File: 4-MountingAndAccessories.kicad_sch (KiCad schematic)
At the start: 16 parts, among them J401 Spring Contact

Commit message: schematics: heavy BOM optimization, many small changes, filling missing fields, improving symbols and everything
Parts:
- H401, H402, H403, H404: Source (none) -> -
- H413: Source (none) -> Mouser
- J401: Source (none) -> TME
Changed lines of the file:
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@@
 	(title_block
 		(title "Mounting, hardware and accessories")
-		(date "2024-02-08")
+		(date "2024-02-15")
 		(rev "3.0")
 		(company "Arx")
@@
 			)
 		)
-		(property "Source" ""
+		(property "Source" "TME"
+			(at 186.69 48.895 0)
+			(effects
+				(font
+					(size 1.27 1.27)
+				)
+				(hide yes)
+			)
+		)
+		(property "Field-1" ""
 			(at 186.69 48.895 0)
 			(effects
@@
 			)
 		)
+		(property "Field-1" ""
+			(at 165.1 115.57 0)
+			(effects
+				(font
+					(size 1.27 1.27)
+				)
+				(hide yes)
+			)
+		)
 		(instances
 			(project "2023_PiezoPreamp"
@@
 			)
 		)
-		(property "Source" ""
+		(property "Source" "-"
+			(at 82.55 64.135 0)
+			(effects
+				(font
+					(size 1.27 1.27)
+				)
+				(hide yes)
+			)
+		)
+		(property "Field-1" ""
 			(at 82.55 64.135 0)
 			(effects
@@
 			)
 		)
-		(property "Source" ""
+		(property "Source" "-"
+			(at 83.82 46.99 0)
+			(effects
+				(font
+					(size 1.27 1.27)
+				)
+				(hide yes)
+			)
+		)
+		(property "Field-1" ""
 			(at 83.82 46.99 0)
 			(effects
@@
 			)
 		)
+		(property "Field-1" ""
+			(at 145.415 106.045 0)
+			(effects
+				(font
+					(size 1.27 1.27)
+				)
+				(hide yes)
+			)
+		)
 		(instances
 			(project "2023_PiezoPreamp"
@@
 			)
 		)
+		(property "Field-1" ""
+			(at 165.1 106.045 0)
+			(effects
+				(font
+					(size 1.27 1.27)
+				)
+				(hide yes)
+			)
+		)
 		(instances
 			(project "2023_PiezoPreamp"
@@
 			)
 		)
-		(property "Source" ""
+		(property "Source" "-"
+			(at 108.585 46.99 0)
+			(effects
+				(font
+					(size 1.27 1.27)
+				)
+				(hide yes)
+			)
+		)
+		(property "Field-1" ""
 			(at 108.585 46.99 0)
 			(effects
@@
 			)
 		)
+		(property "Field-1" ""
+			(at 121.92 116.205 0)
+			(effects
+				(font
+					(size 1.27 1.27)
+				)
+				(hide yes)
+			)
+		)
 		(instances
 			(project "2023_PiezoPreamp"
@@
 		)
 		(property "Source" ""
+			(at 145.415 115.57 0)
+			(effects
+				(font
+					(size 1.27 1.27)
+				)
+				(hide yes)
+			)
+		)
+		(property "Field-1" ""
 			(at 145.415 115.57 0)
 			(effects
@@
 			)
 		)
+		(property "Field-1" ""
+			(at 134.62 64.135 0)
+			(effects
+				(font
+					(size 1.27 1.27)
+				)
+				(hide yes)
+			)
+		)
 		(instances
 			(project "2023_PiezoPreamp"
@@
 			)
 		)
+		(property "Field-1" ""
+			(at 135.255 48.895 0)
+			(effects
+				(font
+					(size 1.27 1.27)
+				)
+				(hide yes)
+			)
+		)
 		(instances
 			(project "2023_PiezoPreamp"
@@
 			)
 		)
-		(property "Source" ""
+		(property "Source" "-"
+			(at 108.585 64.135 0)
+			(effects
+				(font
+					(size 1.27 1.27)
+				)
+				(hide yes)
+			)
+		)
+		(property "Field-1" ""
 			(at 108.585 64.135 0)
 			(effects
@@
 			)
 		)
+		(property "Field-1" ""
+			(at 149.86 64.135 0)
+			(effects
+				(font
+					(size 1.27 1.27)
+				)
+				(hide yes)
+			)
+		)
 		(instances
 			(project "2023_PiezoPreamp"
@@
 			)
 		)
+		(property "Field-1" ""
+			(at 165.1 132.08 0)
+			(effects
+				(font
+					(size 1.27 1.27)
+				)
+				(hide yes)
+			)
+		)
 		(instances
 			(project "2023_PiezoPreamp"
@@
 			)
 		)
-		(property "Source" ""
+		(property "Source" "Mouser"
+			(at 92.075 114.935 0)
+			(effects
+				(font
+					(size 1.27 1.27)
+				)
+				(hide yes)
+			)
+		)
+		(property "Field-1" ""
 			(at 92.075 114.935 0)
 			(effects
@@
 			(at 145.415 132.08 0)
 			(effects
+				(font
+					(size 1.27 1.27)
+				)
+				(hide yes)
+			)
+		)
+		(property "Field-1" ""
+			(at 145.415 132.08 0)
+			(effects

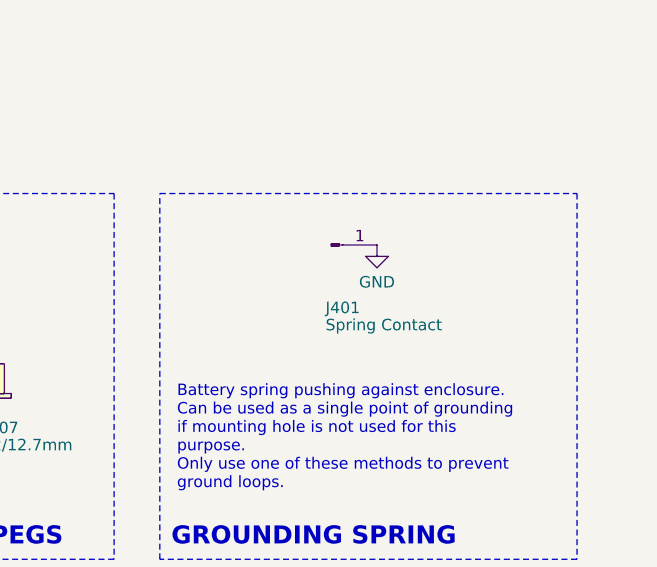
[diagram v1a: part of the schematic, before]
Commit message: aligning schematics to grid, swapping switches as they are on the bottom side now; rough placement of BI section on board
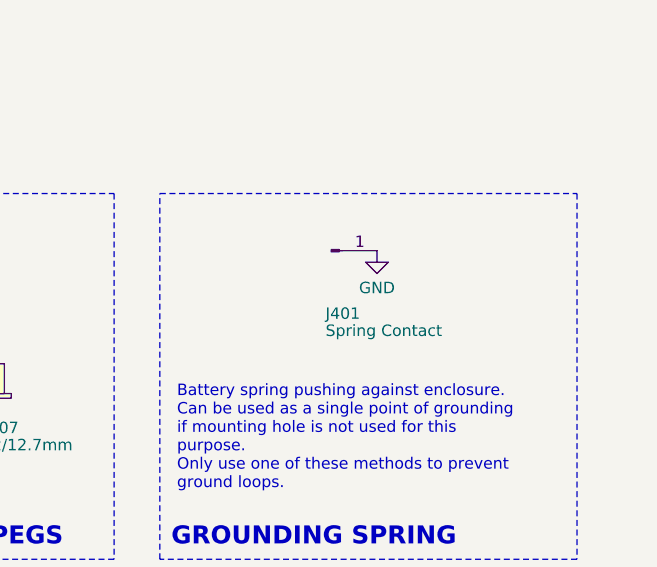
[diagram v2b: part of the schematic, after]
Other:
- moved on the sheet: J401
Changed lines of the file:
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@@
 	(symbol
 		(lib_id "Connector:Conn_01x01_Pin")
-		(at 186.69 48.895 0)
+		(at 186.69 49.53 0)
 		(unit 1)
 		(exclude_from_sim no)
@@
 		(dnp no)
 		(property "Reference" "J401"
-			(at 186.055 55.88 0)
+			(at 186.055 56.515 0)
 			(effects
 				(font
@@
 		)
 		(property "Value" "Spring Contact"
-			(at 186.055 57.785 0)
+			(at 186.055 58.42 0)
 			(effects
 				(font
@@
 		)
 		(property "Footprint" "library:KEYSTONE-5201"
-			(at 186.69 48.895 0)
+			(at 186.69 49.53 0)
 			(effects
 				(font
@@
 		)
 		(property "Datasheet" "https://www.tme.eu/Document/935c8711960b52fec0fbaf2926903193/KEYS5201.pdf"
-			(at 186.69 48.895 0)
+			(at 186.69 49.53 0)
 			(effects
 				(font
@@
 		)
 		(property "Description" ""
-			(at 186.69 48.895 0)
+			(at 186.69 49.53 0)
 			(effects
 				(font
@@
 		)
 		(property "Purpose" "enclosure grounding"
-			(at 186.69 48.895 0)
+			(at 186.69 49.53 0)
 			(effects
 				(font
@@
 		)
 		(property "Mfr" "Keystone"
-			(at 186.69 48.895 0)
+			(at 186.69 49.53 0)
 			(effects
 				(font
@@
 		)
 		(property "Mfr Part #" "5201"
-			(at 186.69 48.895 0)
+			(at 186.69 49.53 0)
 			(effects
 				(font
@@
 		)
 		(property "Mouser Part #" "534-5201"
-			(at 186.69 48.895 0)
+			(at 186.69 49.53 0)
 			(effects
 				(font
@@
 		)
 		(property "LCSC Part #" "-"
-			(at 186.69 48.895 0)
+			(at 186.69 49.53 0)
 			(effects
 				(font
@@
 		)
 		(property "TME Part #" "KEYS5201"
-			(at 186.69 48.895 0)
+			(at 186.69 49.53 0)
 			(effects
 				(font
@@
 		)
 		(property "Source" "TME"
-			(at 186.69 48.895 0)
-			(effects
-				(font
-					(size 1.27 1.27)
-				)
-				(hide yes)
-			)
-		)
-		(property "Field-1" ""
-			(at 186.69 48.895 0)
+			(at 186.69 49.53 0)
 			(effects
 				(font
@@
 			)
 		)
-		(property "Field-1" ""
-			(at 165.1 115.57 0)
-			(effects
-				(font
-					(size 1.27 1.27)
-				)
-				(hide yes)
-			)
-		)
 		(instances
 			(project "2023_PiezoPreamp"
@@
 	(symbol
 		(lib_id "power:GND")
-		(at 191.77 48.895 0)
+		(at 191.77 49.53 0)
 		(unit 1)
 		(exclude_from_sim no)
@@
 		(fields_autoplaced yes)
 		(property "Reference" "#PWR020"
-			(at 191.77 55.245 0)
+			(at 191.77 55.88 0)
 			(effects
 				(font
@@
 		)
 		(property "Value" "GND"
-			(at 191.77 53.0305 0)
+			(at 191.77 53.6655 0)
 			(effects
 				(font
@@
 		)
 		(property "Footprint" ""
-			(at 191.77 48.895 0)
+			(at 191.77 49.53 0)
 			(effects
 				(font
@@
 		)
 		(property "Datasheet" ""
-			(at 191.77 48.895 0)
+			(at 191.77 49.53 0)
 			(effects
 				(font
@@
 		)
 		(property "Description" ""
-			(at 191.77 48.895 0)
+			(at 191.77 49.53 0)
 			(effects
 				(font
@@
 			)
 		)
-		(property "Field-1" ""
-			(at 82.55 64.135 0)
-			(effects
-				(font
-					(size 1.27 1.27)
-				)
-				(hide yes)
-			)
-		)
 		(instances
 			(project "2023_PiezoPreamp"
@@
 			)
 		)
-		(property "Field-1" ""
-			(at 83.82 46.99 0)
-			(effects
-				(font
-					(size 1.27 1.27)
-				)
-				(hide yes)
-			)
-		)
 		(pin "1"
 		)
@@
 			)
 		)
-		(property "Field-1" ""
-			(at 145.415 106.045 0)
-			(effects
-				(font
-					(size 1.27 1.27)
-				)
-				(hide yes)
-			)
-		)
 		(instances
 			(project "2023_PiezoPreamp"
@@
 			)
 		)
-		(property "Field-1" ""
-			(at 165.1 106.045 0)
-			(effects
-				(font
-					(size 1.27 1.27)
-				)
-				(hide yes)
-			)
-		)
 		(instances
 			(project "2023_PiezoPreamp"
@@
 			)
 		)
-		(property "Field-1" ""
-			(at 108.585 46.99 0)
-			(effects
-				(font
-					(size 1.27 1.27)
-				)
-				(hide yes)
-			)
-		)
 		(instances
 			(project "2023_PiezoPreamp"
@@
 			)
 		)
-		(property "Field-1" ""
-			(at 121.92 116.205 0)
-			(effects
-				(font
-					(size 1.27 1.27)
-				)
-				(hide yes)
-			)
-		)
 		(instances
 			(project "2023_PiezoPreamp"
@@
 			)
 		)
-		(property "Field-1" ""
-			(at 145.415 115.57 0)
-			(effects
-				(font
-					(size 1.27 1.27)
-				)
-				(hide yes)
-			)
-		)
 		(instances
 			(project "2023_PiezoPreamp"
@@
 			)
 		)
-		(property "Field-1" ""
-			(at 134.62 64.135 0)
-			(effects
-				(font
-					(size 1.27 1.27)
-				)
-				(hide yes)
-			)
-		)
 		(instances
 			(project "2023_PiezoPreamp"
@@
 			)
 		)
-		(property "Field-1" ""
-			(at 135.255 48.895 0)
-			(effects
-				(font
-					(size 1.27 1.27)
-				)
-				(hide yes)
-			)
-		)
 		(instances
 			(project "2023_PiezoPreamp"
@@
 			)
 		)
-		(property "Field-1" ""
-			(at 108.585 64.135 0)
-			(effects
-				(font
-					(size 1.27 1.27)
-				)
-				(hide yes)
-			)
-		)
 		(instances
 			(project "2023_PiezoPreamp"
@@
 			)
 		)
-		(property "Field-1" ""
-			(at 149.86 64.135 0)
-			(effects
-				(font
-					(size 1.27 1.27)
-				)
-				(hide yes)
-			)
-		)
 		(instances
 			(project "2023_PiezoPreamp"
@@
 			)
 		)
-		(property "Field-1" ""
-			(at 165.1 132.08 0)
-			(effects
-				(font
-					(size 1.27 1.27)
-				)
-				(hide yes)
-			)
-		)
 		(instances
 			(project "2023_PiezoPreamp"
@@
 			)
 		)
-		(property "Field-1" ""
-			(at 92.075 114.935 0)
-			(effects
-				(font
-					(size 1.27 1.27)
-				)
-				(hide yes)
-			)
-		)
 		(instances
 			(project "2023_PiezoPreamp"
@@
 			(at 145.415 132.08 0)
 			(effects
-				(font
-					(size 1.27 1.27)
-				)
-				(hide yes)
-			)
-		)
-		(property "Field-1" ""
-			(at 145.415 132.08 0)
-			(effects
